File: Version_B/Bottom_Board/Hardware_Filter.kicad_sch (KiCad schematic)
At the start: 38 parts, among them U1 LM324DR, U2 LM324DR

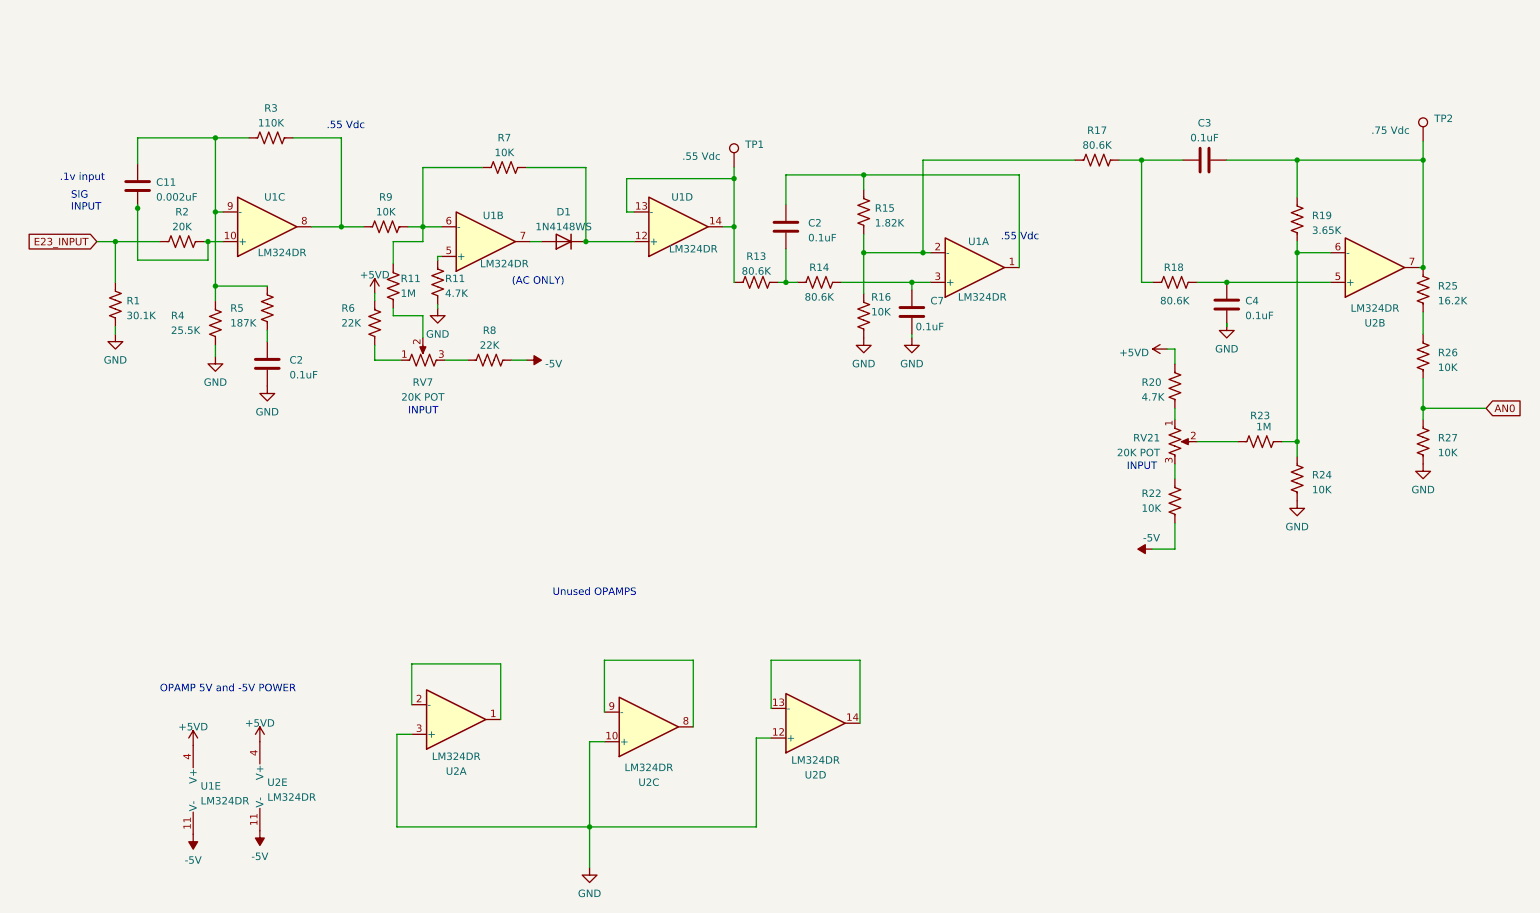
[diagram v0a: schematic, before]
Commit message: fixed directory overwrite
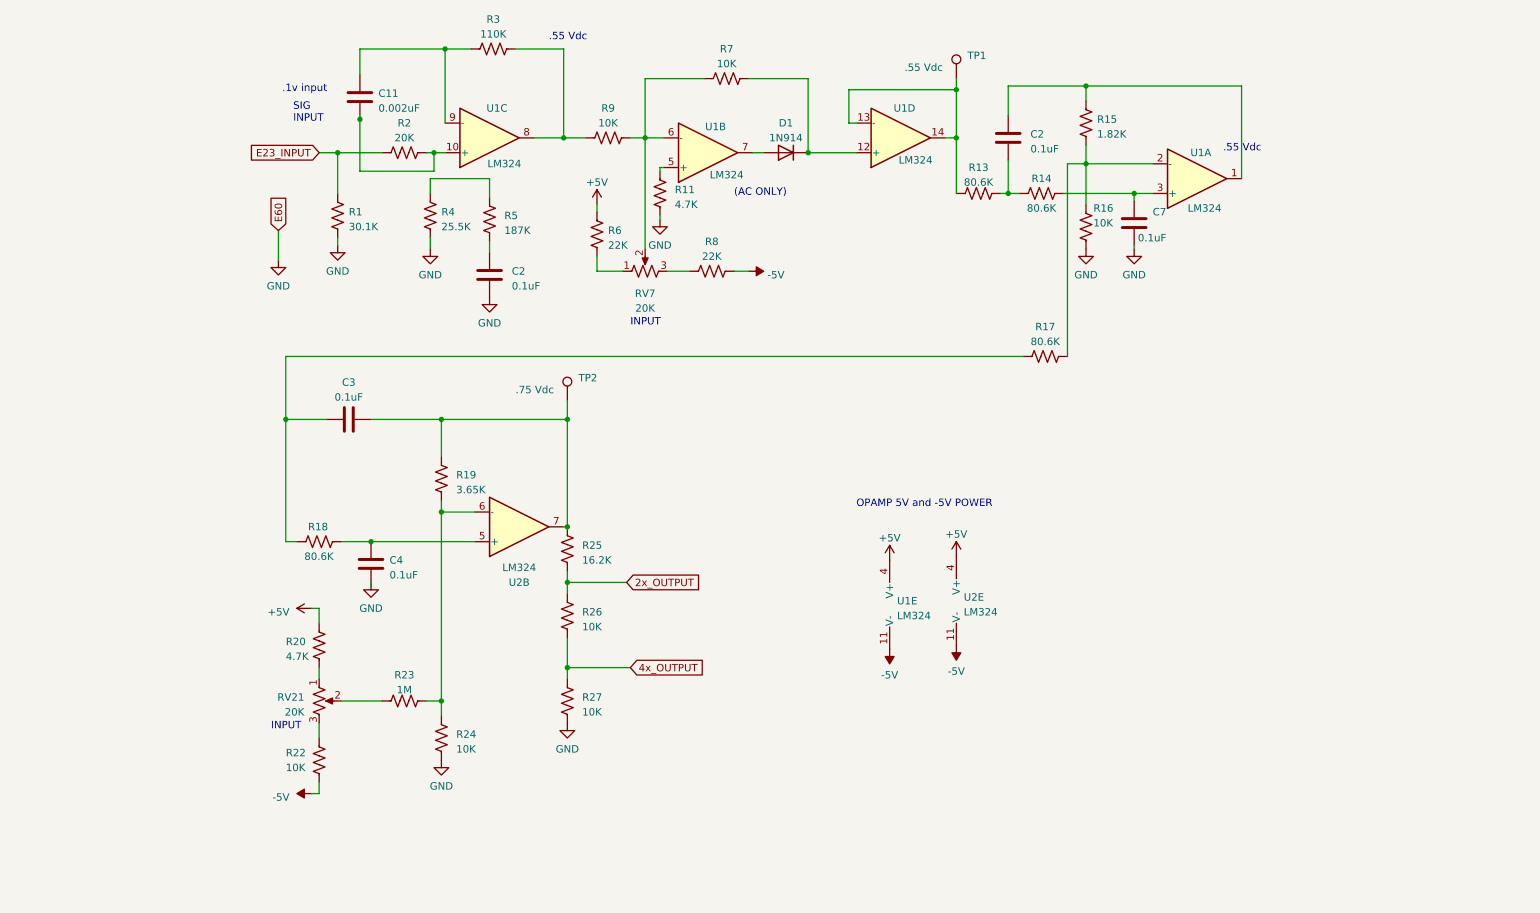
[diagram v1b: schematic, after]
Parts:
- removed R11: 1M, Resistor_SMD:R_0603_1608Metric, symbol Device:R_US
- removed unit 1 of U2
- removed unit 4 of U2
- removed unit 3 of U2
- D1: value 1N4148WS -> 1N914; footprint bot_lib:Diode_1N4148WS -> Diode_SMD:D_0603_1608Metric
- RV21, RV7: value 20K POT -> 20K; footprint bot_lib:Potentiometer_Bourns_3386P_Vertical -> Potentiometer_THT:Potentiometer_Bourns_3386P_Vertical
- U1, U2: value LM324DR -> LM324
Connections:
- net at R7.1, R9.2, U1.6 (-): now also RV7.2
- net at C11.1, R3.1, U1.9 (-): no longer R4.1, R5.1
- net 2x_OUTPUT: now reaches R25.1, R26.2
- net +5VD renamed +5V
- net AN0 renamed 4x_OUTPUT
- new net: R4.1, R5.1
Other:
- note removed: "Unused OPAMPS"
- company: Secured Solutions Group -> (none)
- title: Current Monitoring System (Bottom Board) -> (none)
- moved on the sheet: C11, C2, C3, C4, C7, D1, R1, R11, R13, R14, R15, R16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
